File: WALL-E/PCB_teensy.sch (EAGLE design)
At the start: 30 parts

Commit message: update
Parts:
- removed TP4, TP5, TP6, TP7, TP8, TP9: PTR1B2,54, testpad:PTR1B2,54
- removed U$3: SD-22-03-2031, WALL-E_Parts:SD-22-03-2031
- removed _1: TEENSY, WALL-E_Parts:TEENSY
- added U$1: TEENSY_3.5/3.6, WALL-E_Parts:TEENSY_3.5/3.6
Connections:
- removed net CLK: TP5.TP, U$3.P$4, _1._B3
- removed net CS: TP8.TP, U$3.P$1, _1._B0
- removed net D0: J1.3, _1._D0
- removed net D1: J1.4, _1._D1
- removed net D2: J2.3, _1._D2
- removed net D3: J2.4, _1._D3
- removed net D4: J3.3, _1._D4
- removed net D5: J3.4, _1._D5
- removed net D6: J4.3, _1._D6
- removed net D7: J4.4, _1._D7
- removed net DI: TP7.TP, U$3.P$2, _1._B2
- removed net DO: TP6.TP, U$3.P$3, _1._B1
- removed net N$21: J5.3
- removed net N$22: J5.4
- new net 0/RX: J1.3, U$1.0/RX
- new net 1/TX: J1.4, U$1.1/TX
- net 3.3V: now also U$1.3V3, U$1.3V3_2, U$1.VIN; no longer TP9.TP, U$3.P$6
- net 5V: no longer _1.5V, _1._5V2
- net GND: now also U$1.GND, U$1.GND2, U$1.GND3; no longer TP4.TP, U$3.P$5, _1._GND, _1._GND1
- net N$4: now also U$1.RESET; no longer _1._RST

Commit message: updated schematic
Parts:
- added J10, J11, J12, J7, J8, J9: (no value), con-amp:MTA04-100
- added J13: (no value), con-amp:MTA04-156
- added J6: (no value), con-amp:MTA03-100
- added JP1, JP2: (no value), adafruit:PINHD-1X20
- added LED2: (no value), led:LEDCHIP-LED0805
- added R1: (no value), adafruit:R-US_R0805
- added TP4: PTR1B2,54, testpad:PTR1B2,54
- added U$3: 2.1MMJACKTHM, adafruit:2.1MMJACKTHM
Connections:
- new net 10U: JP1.2, JP2.6, U$1.10/CS, U$1.A10
- new net 11U: JP2.7, U$1.A11
- new net 14U: JP1.16, U$1.14/A0
- new net 15U: JP1.17, U$1.15/A1
- new net 16U: JP1.18, U$1.16/A2
- new net 17U: JP2.1, U$1.17/A3
- new net 20U: JP2.2, U$1.20/A6
- new net 21U: JP2.3, U$1.21/A7
- new net 22U: JP2.4, U$1.22/A8
- new net 23U: JP2.5, U$1.23/A9
- new net 24: J4.3, U$1.24
- new net 25: J4.4, U$1.25
- new net 26: J5.3, U$1.26
- new net 27: J5.4, U$1.27
- new net 28U: JP1.3, U$1.28
- new net 29U: JP1.4, U$1.29
- new net 3.3V_LOW: JP1.19, U$1.3V3_LO
- new net 30U: JP1.5, U$1.30
- new net 31U: JP1.6, U$1.31/A12
- new net 32U: JP1.7, U$1.32/A13
- new net 33U: JP1.8, U$1.33/A14
- new net 34U: JP1.9, U$1.34/A15
- new net 35U: JP1.10, U$1.35/A16
- new net 36U: JP1.11, U$1.36/A17
- new net 37U: JP1.12, U$1.37/A18
- new net 39U: JP1.13, U$1.39/A20
- new net 5: J2.3, U$1.5
- new net 6: J2.4, U$1.6
- new net 7: J3.3, U$1.7
- new net 8: J3.4, U$1.8
- new net 9U: JP1.1, U$1.9/CS
- new net AGND: JP1.20, U$1.AGND
- new net ALARMPIN: J6.3, U$1.2
- new net DAC0: JP1.14, U$1.A21/DAC0
- new net DAC1: JP1.15, U$1.A22/DAC1
- new net MISO_0: J13.4, U$1.12/MISO
- new net MOSI_0: J13.3, U$1.11/MOSI
- new net N$17: R1.2, U$1.13/SCK
- new net N$18: LED2.A, R1.1
- new net SCL0: J11.3, J8.3, U$1.19/A5/SCL
- new net SCL1: J10.3, J7.3
- new net SCL2: J12.3, J9.3, U$1.3/CANTX
- new net SDA0: J11.4, J8.4, U$1.18/A4/SDA
- new net SDA1: J10.4, J7.4
- new net SDA2: J12.4, J9.4, U$1.38/A19, U$1.4/CANRX
- net +12V: now also TP4.TP, U$3.RING
- net 3.3V: now also J10.1, J11.1, J12.1, J13.1, J6.1, J7.1, J8.1, J9.1, R2.2
- net 5V: no longer R2.2
- net GND: now also J10.2, J11.2, J12.2, J13.2, J6.2, J7.2, J8.2, J9.2, JP2.8, LED2.C, U$3.RING_SW, U$3.TIP

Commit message: started on the layout
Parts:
- removed J13: (no value), con-amp:MTA04-156
- added J14: (no value), con-amp:MTA04-100
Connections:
- net 3.3V: now also J14.1; no longer J13.1
- net GND: now also J14.2; no longer J13.2
- net MISO_0: now also J14.4; no longer J13.4
- net MOSI_0: now also J14.3; no longer J13.3
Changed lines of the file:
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@@
 <part name="J11" library="con-amp" library_urn="urn:adsk.eagle:library:127" deviceset="MTA04-100" device=""/>
 <part name="J12" library="con-amp" library_urn="urn:adsk.eagle:library:127" deviceset="MTA04-100" device=""/>
-<part name="J13" library="con-amp" library_urn="urn:adsk.eagle:library:127" deviceset="MTA04-156" device=""/>
 <part name="JP1" library="adafruit" library_urn="urn:adsk.eagle:library:420" deviceset="PINHD-1X20" device=""/>
 <part name="JP2" library="adafruit" library_urn="urn:adsk.eagle:library:420" deviceset="PINHD-1X20" device=""/>
+<part name="J14" library="con-amp" library_urn="urn:adsk.eagle:library:127" deviceset="MTA04-100" device=""/>
 </parts>
 <sheets>
@@
 <instance part="J11" gate="G$1" x="71.12" y="86.36"/>
 <instance part="J12" gate="G$1" x="91.44" y="86.36"/>
-<instance part="J13" gate="G$3" x="71.12" y="50.8"/>
 <instance part="JP1" gate="A" x="-63.5" y="-25.4" rot="R270"/>
 <instance part="JP2" gate="A" x="-114.3" y="-7.62" rot="R180"/>
+<instance part="J14" gate="G$1" x="99.06" y="50.8"/>
 </instances>
 <busses>
@@
 </segment>
 <segment>
-<pinref part="J13" gate="G$3" pin="2"/>
-<wire x1="73.66" y1="48.26" x2="73.66" y2="43.18" width="0.1524" layer="91"/>
-<label x="73.66" y="38.1" size="1.778" layer="95"/>
-</segment>
-<segment>
 <pinref part="JP2" gate="A" pin="8"/>
 <wire x1="-111.76" y1="-12.7" x2="-104.14" y2="-12.7" width="0.1524" layer="91"/>
@@
 <wire x1="-111.76" y1="17.78" x2="-104.14" y2="17.78" width="0.1524" layer="91"/>
 <label x="-104.14" y="17.78" size="1.778" layer="95"/>
+</segment>
+<segment>
+<pinref part="J14" gate="G$1" pin="2"/>
+<wire x1="99.06" y1="48.26" x2="99.06" y2="40.64" width="0.1524" layer="91"/>
+<label x="96.52" y="35.56" size="1.778" layer="95"/>
 </segment>
 </net>
@@
 </segment>
 <segment>
-<pinref part="J13" gate="G$3" pin="1"/>
-<wire x1="71.12" y1="48.26" x2="71.12" y2="43.18" width="0.1524" layer="91"/>
-<label x="68.58" y="40.64" size="1.778" layer="95"/>
+<pinref part="J14" gate="G$1" pin="1"/>
+<wire x1="96.52" y1="48.26" x2="96.52" y2="40.64" width="0.1524" layer="91"/>
+<label x="93.98" y="38.1" size="1.778" layer="95"/>
 </segment>
 </net>
@@
 <net name="MOSI_0" class="0">
 <segment>
-<pinref part="J13" gate="G$3" pin="3"/>
-<wire x1="76.2" y1="48.26" x2="76.2" y2="43.18" width="0.1524" layer="91"/>
-<label x="76.2" y="40.64" size="1.778" layer="95"/>
-</segment>
-<segment>
 <pinref part="U$1" gate="G$1" pin="11/MOSI"/>
 <wire x1="-30.48" y1="33.02" x2="-35.56" y2="33.02" width="0.1524" layer="91"/>
 <label x="-35.56" y="33.02" size="1.778" layer="95"/>
 </segment>
+<segment>
+<pinref part="J14" gate="G$1" pin="3"/>
+<wire x1="101.6" y1="48.26" x2="101.6" y2="40.64" width="0.1524" layer="91"/>
+<label x="101.6" y="38.1" size="1.778" layer="95"/>
+</segment>
 </net>
 <net name="MISO_0" class="0">
-<segment>
-<pinref part="J13" gate="G$3" pin="4"/>
-<wire x1="78.74" y1="48.26" x2="78.74" y2="43.18" width="0.1524" layer="91"/>
-<label x="81.28" y="38.1" size="1.778" layer="95"/>
-</segment>
 <segment>
 <pinref part="U$1" gate="G$1" pin="12/MISO"/>
@@
 <label x="-35.56" y="30.48" size="1.778" layer="95"/>
 </segment>
-</net>
+<segment>
+<pinref part="J14" gate="G$1" pin="4"/>
+<wire x1="104.14" y1="48.26" x2="104.14" y2="40.64" width="0.1524" layer="91"/>
+<label x="104.14" y="35.56" size="1.778" layer="95"/>
+</segment>
+</net>

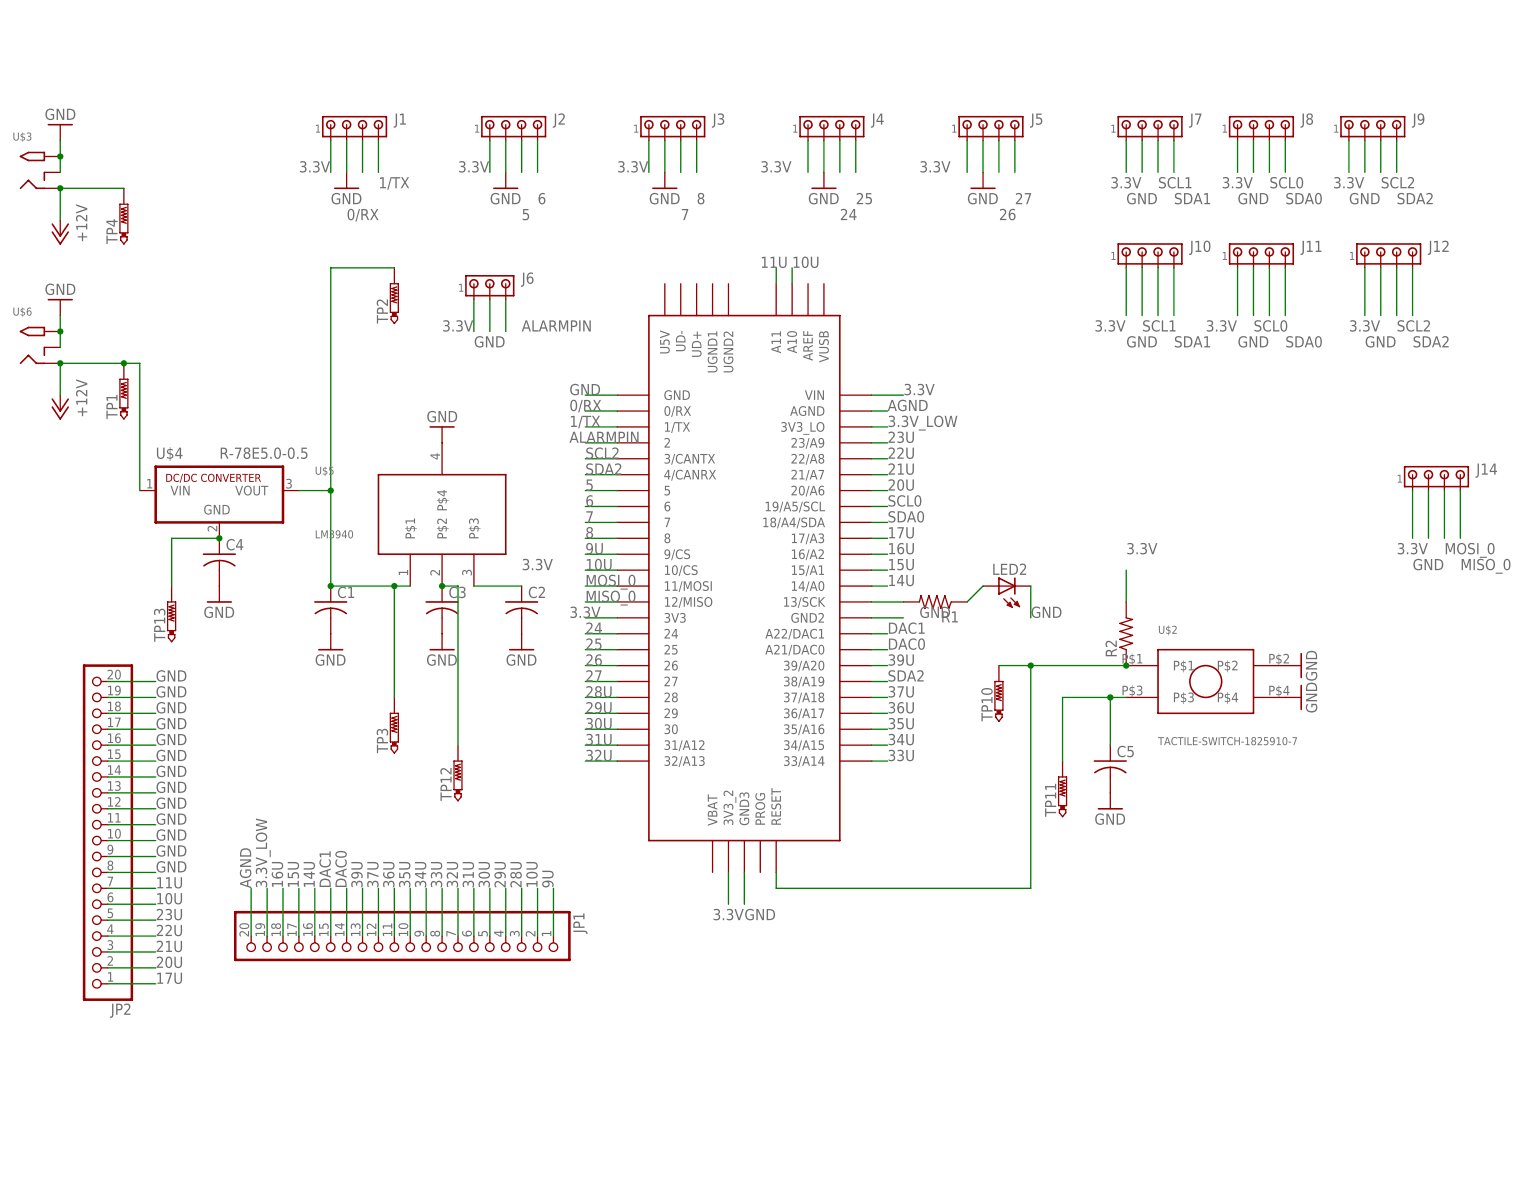
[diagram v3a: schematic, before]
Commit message: added some pull up resistor and added 5v power to teensy with a jumper
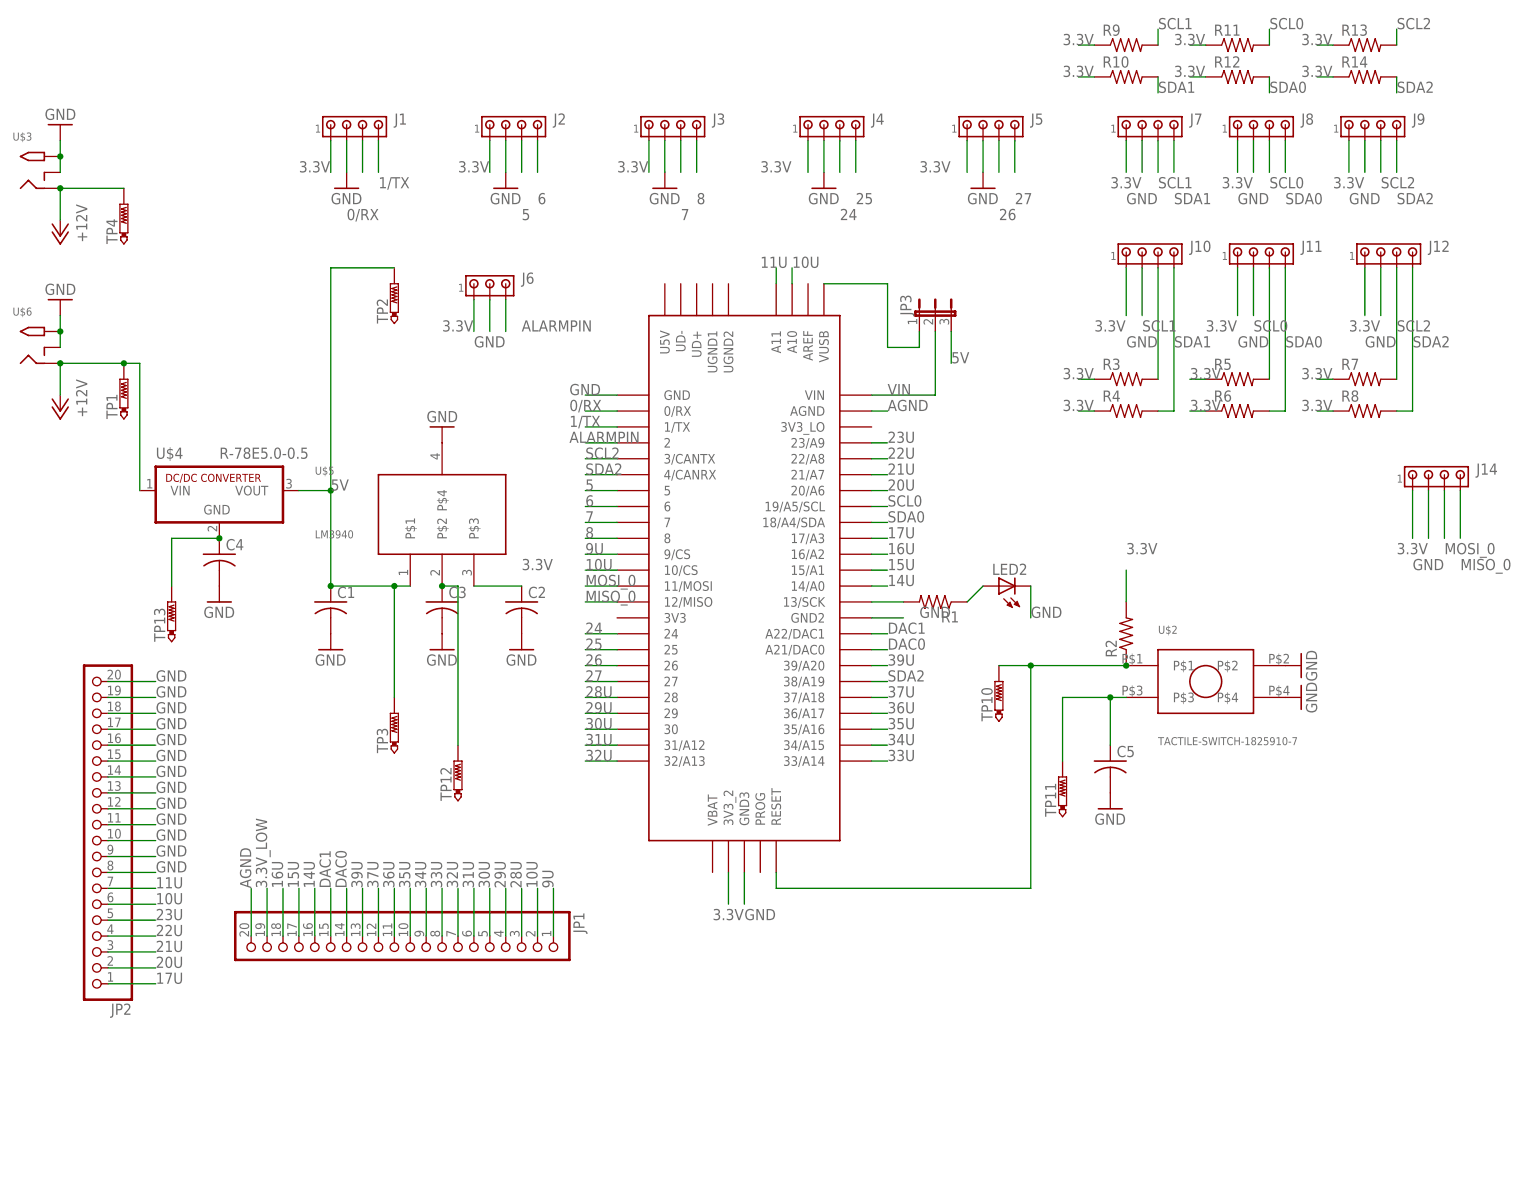
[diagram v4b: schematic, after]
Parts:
- added JP3: (no value), jumper:JP2W
- added R10, R11, R12, R13, R14, R3, R4, R5, R6, R7, R8, R9: (no value), adafruit:R-US_R0805
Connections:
- new net N$2: JP3.1, U$1.VUSB
- new net VIN: JP3.2, U$1.VIN
- net 3.3V: now also R10.1, R11.1, R12.1, R13.1, R14.1, R3.1, R4.1, R5.1, R6.1, R7.1, R8.1, R9.1; no longer U$1.3V3, U$1.VIN
- net 3.3V_LOW: no longer U$1.3V3_LO
- net 5V: now also JP3.3
- net SCL0: now also R11.2, R5.2
- net SCL1: now also R3.2, R9.2
- net SCL2: now also R13.2, R7.2
- net SDA0: now also R12.2, R6.2
- net SDA1: now also R10.2, R4.2
- net SDA2: now also R14.2, R8.2

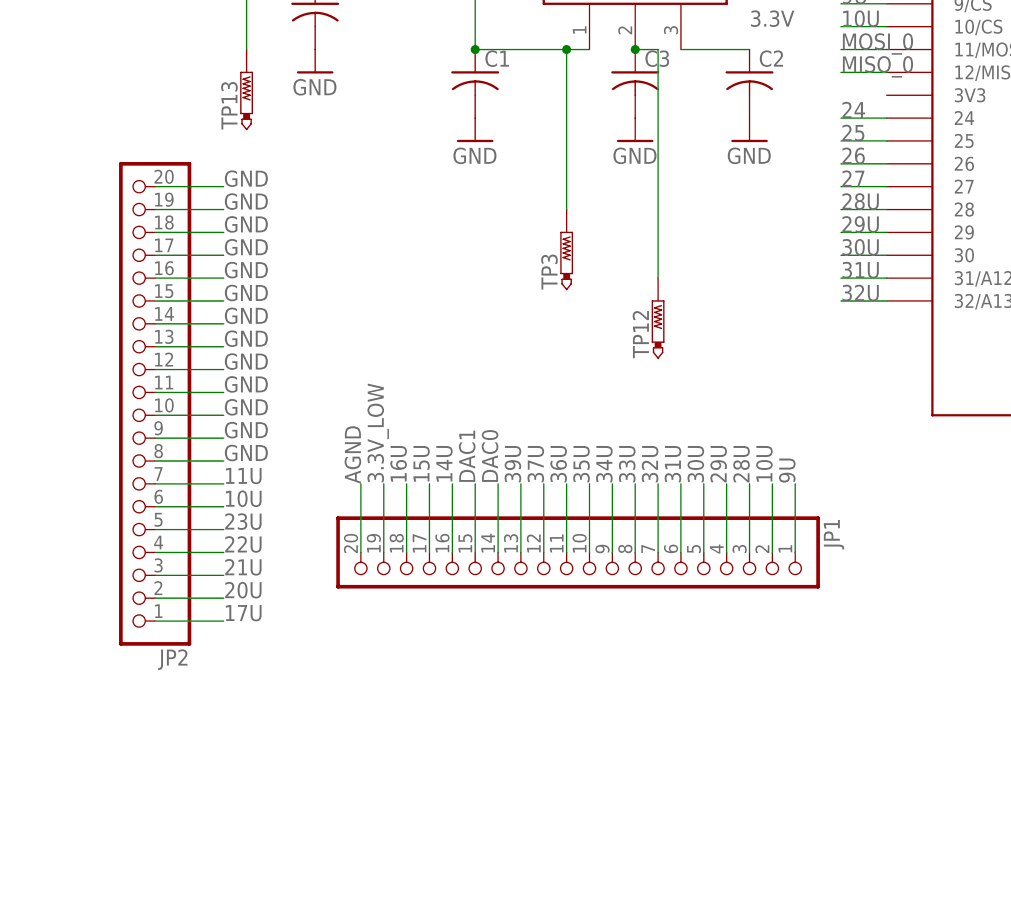
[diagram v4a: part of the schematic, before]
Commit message: Rewired the JP1 pins to be physically closer to the teensy board.
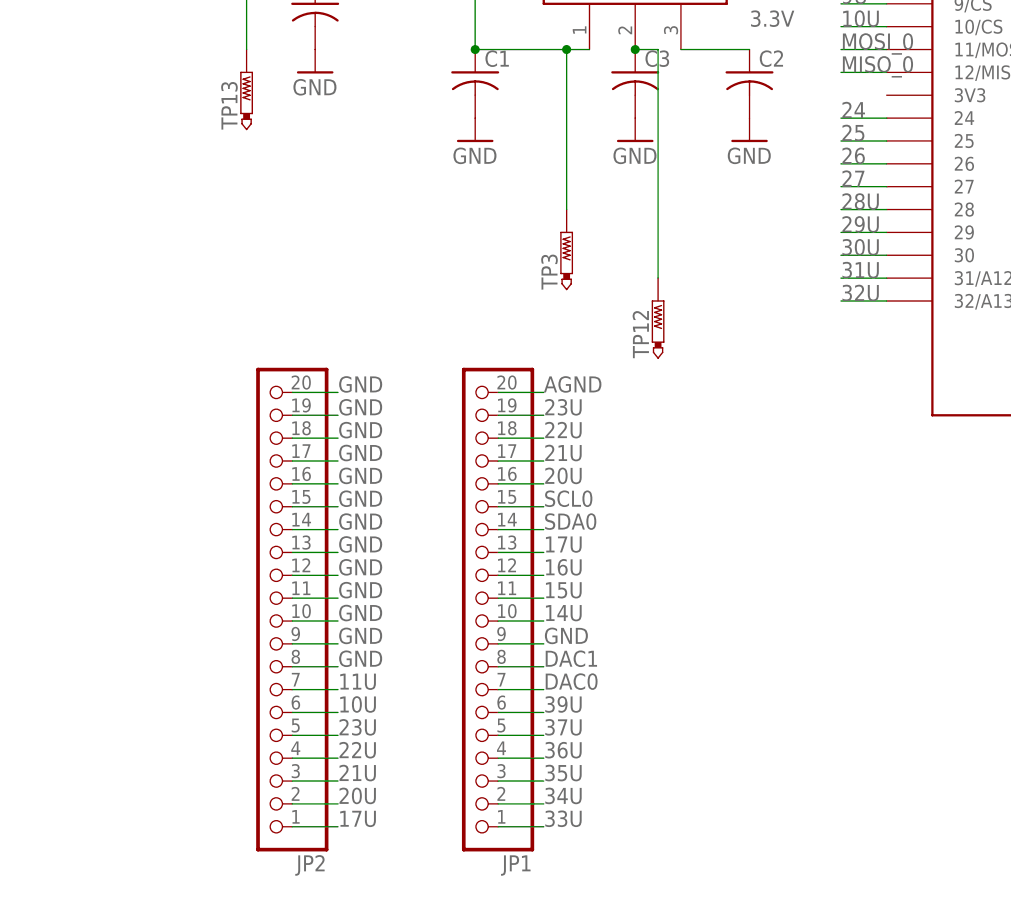
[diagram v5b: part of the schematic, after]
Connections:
- removed net 3.3V_LOW: JP1.19
- net 10U: no longer JP1.2
- net 14U: now also JP1.10; no longer JP1.16
- net 15U: now also JP1.11; no longer JP1.17
- net 16U: now also JP1.12; no longer JP1.18
- net 17U: now also JP1.13
- net 20U: now also JP1.16
- net 21U: now also JP1.17
- net 22U: now also JP1.18
- net 23U: now also JP1.19
- net 28U: no longer JP1.3
- net 29U: no longer JP1.4
- net 30U: no longer JP1.5
- net 31U: no longer JP1.6
- net 32U: no longer JP1.7
- net 33U: now also JP1.1; no longer JP1.8
- net 34U: now also JP1.2; no longer JP1.9
- net 35U: now also JP1.3; no longer JP1.10
- net 36U: now also JP1.4; no longer JP1.11
- net 37U: now also JP1.5; no longer JP1.12
- net 39U: now also JP1.6; no longer JP1.13
- net 9U: no longer JP1.1
- net DAC0: now also JP1.7; no longer JP1.14
- net DAC1: now also JP1.8; no longer JP1.15
- net GND: now also JP1.9, JP2.10, JP2.11, JP2.12, JP2.13, JP2.14, JP2.15, JP2.16, JP2.17, JP2.18, JP2.19, JP2.20, JP2.9
- net SCL0: now also JP1.15
- net SDA0: now also JP1.14
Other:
- moved on the sheet: JP1, JP2
